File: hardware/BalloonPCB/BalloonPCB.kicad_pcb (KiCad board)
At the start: 2 copper layers, 106.7 x 86.4 mm, 5 parts, among them P1 BMP180_HEADER, P2 GPS_HEADER, P3 ACCEL_HEADER, P4 CONN_01X24, U1 Teensy3.5

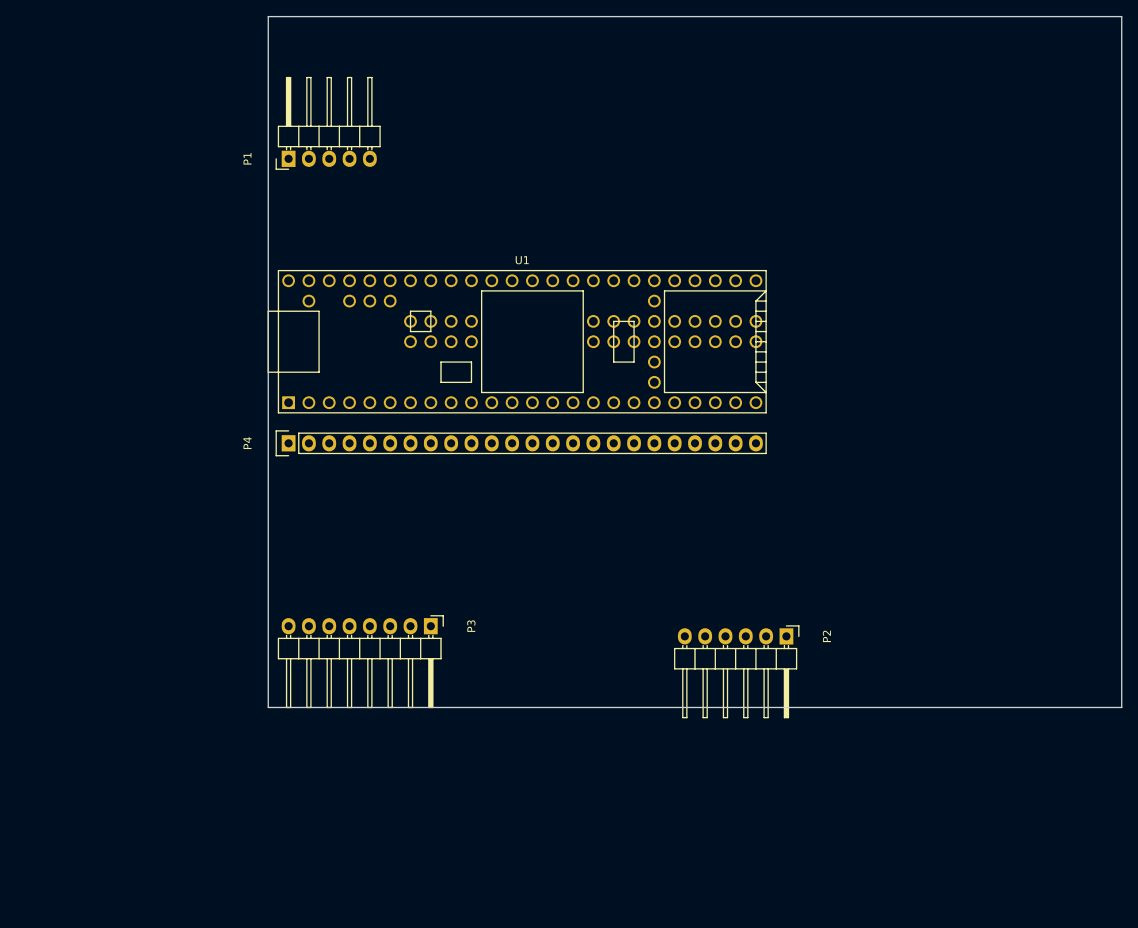
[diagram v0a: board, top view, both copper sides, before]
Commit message: First routing pass, everything except radio
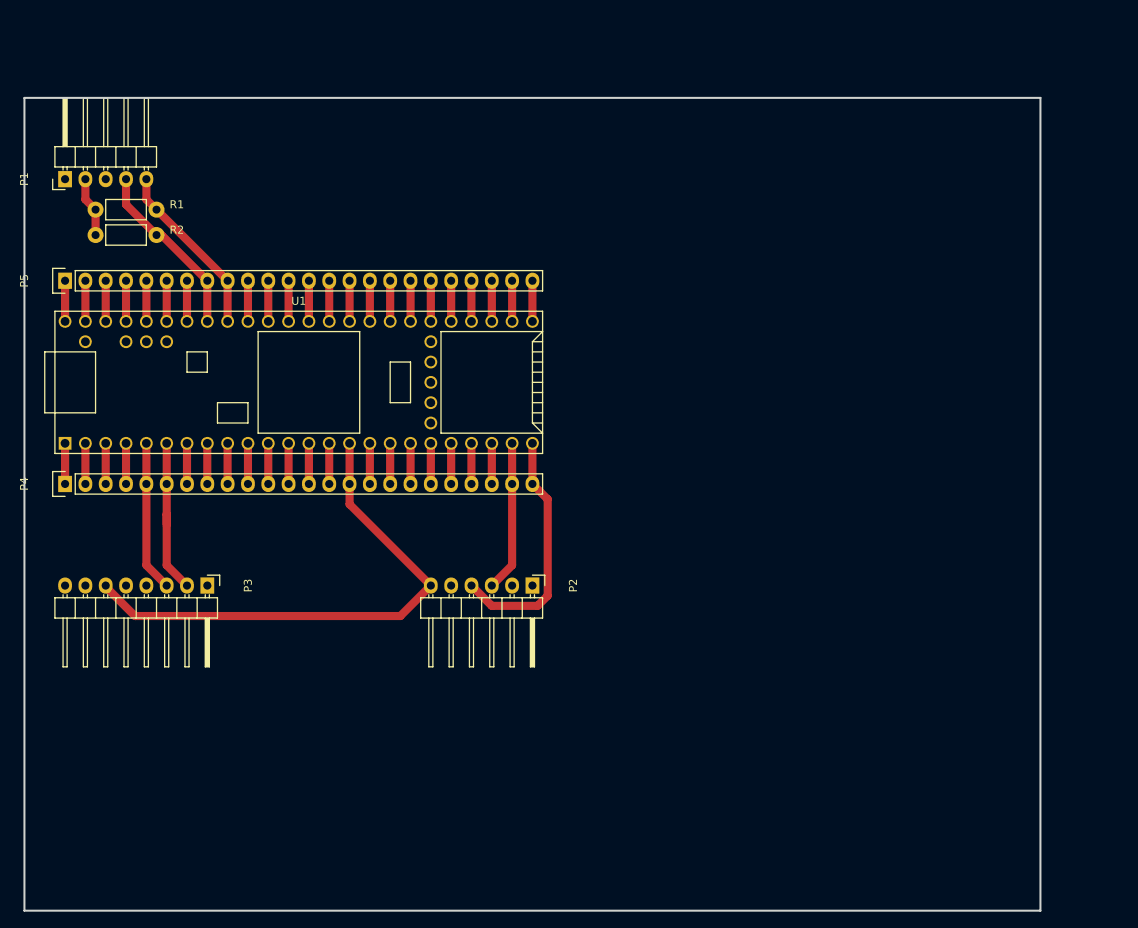
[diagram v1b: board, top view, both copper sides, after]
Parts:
- added P5: CONN_01X24, Pin_Headers:Pin_Header_Straight_1x24, F.Cu at (55.9, 73.7)
- added R1: 3.3k, Resistors_THT:Resistor_Horizontal_RM7mm, F.Cu at (59.7, 64.8)
- added R2: 3.3k, Resistors_THT:Resistor_Horizontal_RM7mm, F.Cu at (59.7, 67.9)
- moved P2 32.4 mm to (114.3, 111.8)
- moved P3 28.4 mm to (73.7, 111.8)
- moved U1 28.4 mm to (85.1, 86.4)
- moved P4 28.4 mm to (55.9, 99.1)
- moved P1 28.1 mm to (55.9, 61.0)
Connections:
- P3 pad 2: SDA0 -> SDA2
- P3 pad 3: SCL0 -> SCL2
- P4 pad 1: Net-(P4-Pad1) -> GND
- P4 pad 5: Net-(P4-Pad5) -> SCL2
- P4 pad 6: Net-(P4-Pad6) -> SDA2
- U1 pad 1: Net-(P4-Pad1) -> GND
- U1 pad 26: Net-(U1-Pad26) -> +3V3
- U1 pad 45: Net-(U1-Pad45) -> SDA0
- U1 pad 46: Net-(U1-Pad46) -> SCL0
- U1 pad 5: Net-(P4-Pad5) -> SCL2
- U1 pad 6: Net-(P4-Pad6) -> SDA2
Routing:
- net +3V3: track 0.00 -> 73.4 mm
- net GPS_RXD: track 0.00 -> 30.9 mm
- net SCL0: track 0.00 -> 22.4 mm
- net SDA0: track 0.00 -> 22.0 mm
- net SDA2: track 0.00 -> 20.1 mm
- net GPS_TXD: track 0.00 -> 18.8 mm
- net SCL2: track 0.00 -> 18.8 mm
- net GND: track 0.00 -> 10.2 mm
- net Net-(P5-Pad7): track 0.00 -> 5.08 mm
- net Net-(P5-Pad6): track 0.00 -> 5.08 mm
- net Net-(P5-Pad5): track 0.00 -> 5.08 mm
- net Net-(P5-Pad4): track 0.00 -> 5.08 mm
- net Net-(P5-Pad3): track 0.00 -> 5.08 mm
- net Net-(P5-Pad24): track 0.00 -> 5.08 mm
- net Net-(P5-Pad23): track 0.00 -> 5.08 mm
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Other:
- board size 106.7 x 86.4 mm -> 127 x 101.6 mm
- net class Default: trace_width 0.254 -> 1.016
- net class Power added: clearance 0.254, trace_width 1.016, via_dia 0.762, via_drill 0.3302
- net class Signal added: clearance 0.254, trace_width 0.508, via_dia 0.762, via_drill 0.3302
- net class SmallSig added: clearance 0.254, trace_width 0.254, via_dia 0.762, via_drill 0.3302

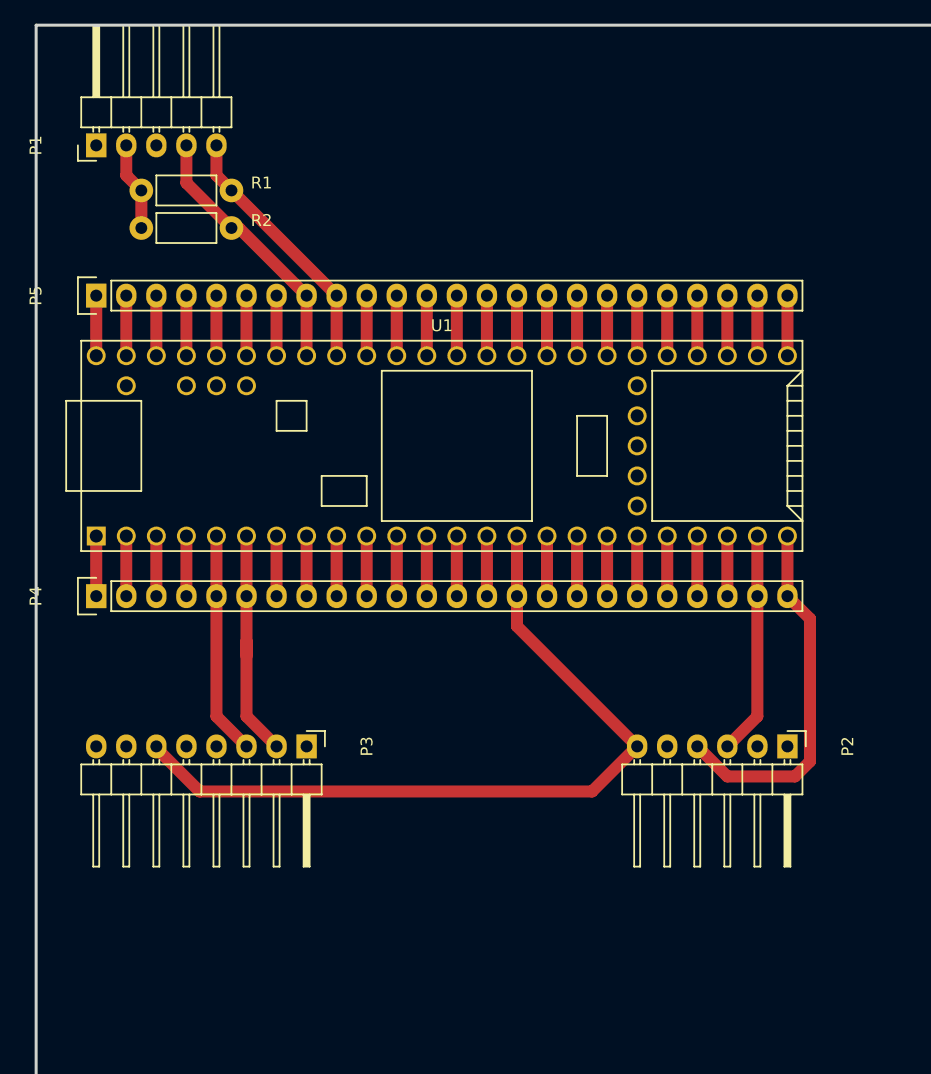
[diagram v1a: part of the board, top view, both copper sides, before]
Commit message: PCB signals routed
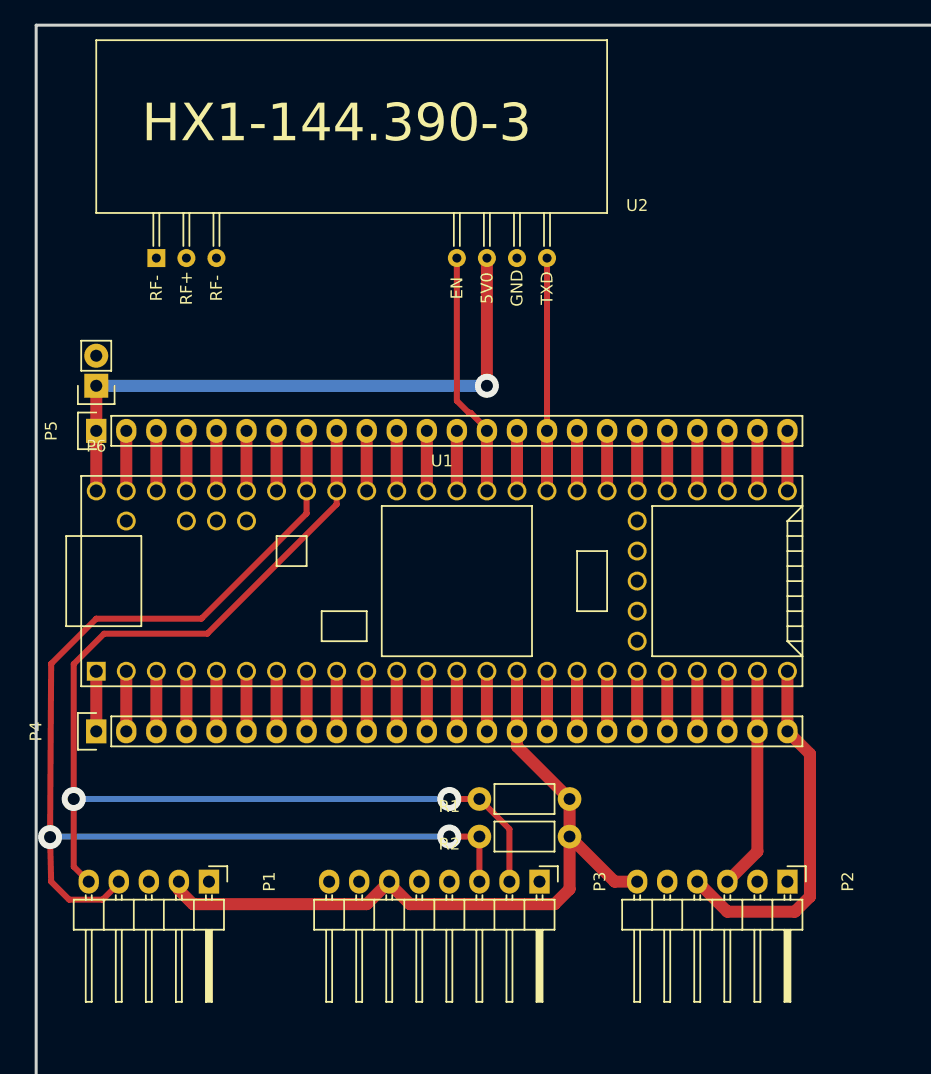
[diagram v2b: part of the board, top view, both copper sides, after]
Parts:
- added P6: 5VDC_HEADER, Pin_Headers:Pin_Header_Straight_1x02, F.Cu at (55.9, 81.3)
- added U2: HX1, HX1:HX1, F.Cu at (55.9, 66.7)
- moved P1 63.0 mm to (65.4, 123.2), turned to 270 degrees
- moved R1 62.9 mm to (95.9, 116.2), turned to 180 degrees
- moved R2 62.9 mm to (95.9, 119.4), turned to 180 degrees
- moved P3 22.8 mm to (93.3, 123.2)
- moved P5 11.4 mm to (55.9, 85.1)
- moved U1 11.4 mm to (85.1, 97.8)
- moved P2 11.4 mm to (114.3, 123.2)
- moved P4 11.4 mm to (55.9, 110.5)
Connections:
- net Net-(P5-Pad1) renamed +5V
- net Net-(P5-Pad14) renamed TX_EN
- net Net-(P5-Pad16) renamed TXD
- P3 pad 2: SDA2 -> SDA0
- P3 pad 3: SCL2 -> SCL0
- P5 pad 3: Net-(P5-Pad3) -> +3V3
- U1 pad 51: Net-(P5-Pad3) -> +3V3
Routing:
- net SCL0: track 22.4 -> 99.6 mm, vias 0 -> 2
- net SDA0: track 22.0 -> 95.4 mm, vias 0 -> 2
- net +5V: track 5.08 -> 52.7 mm, vias 0 -> 1
- net TX_EN: track 5.08 -> 20.8 mm
- net SDA2: track 20.1 -> 5.08 mm
- net TXD: track 5.08 -> 19.7 mm
- net SCL2: track 18.8 -> 5.08 mm
- net Net-(P5-Pad3): track 5.08 -> 0.00 mm
- net +3V3: track 73.4 -> 69.0 mm
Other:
- net class Default: via_dia 0.762 -> 2.032; via_drill 0.3302 -> 1.016
- net class Power: via_dia 0.762 -> 2.032; via_drill 0.3302 -> 1.016
- net class Signal: via_dia 0.762 -> 2.032; via_drill 0.3302 -> 1.016
- net class SmallSig: via_dia 0.762 -> 2.032; via_drill 0.3302 -> 1.016

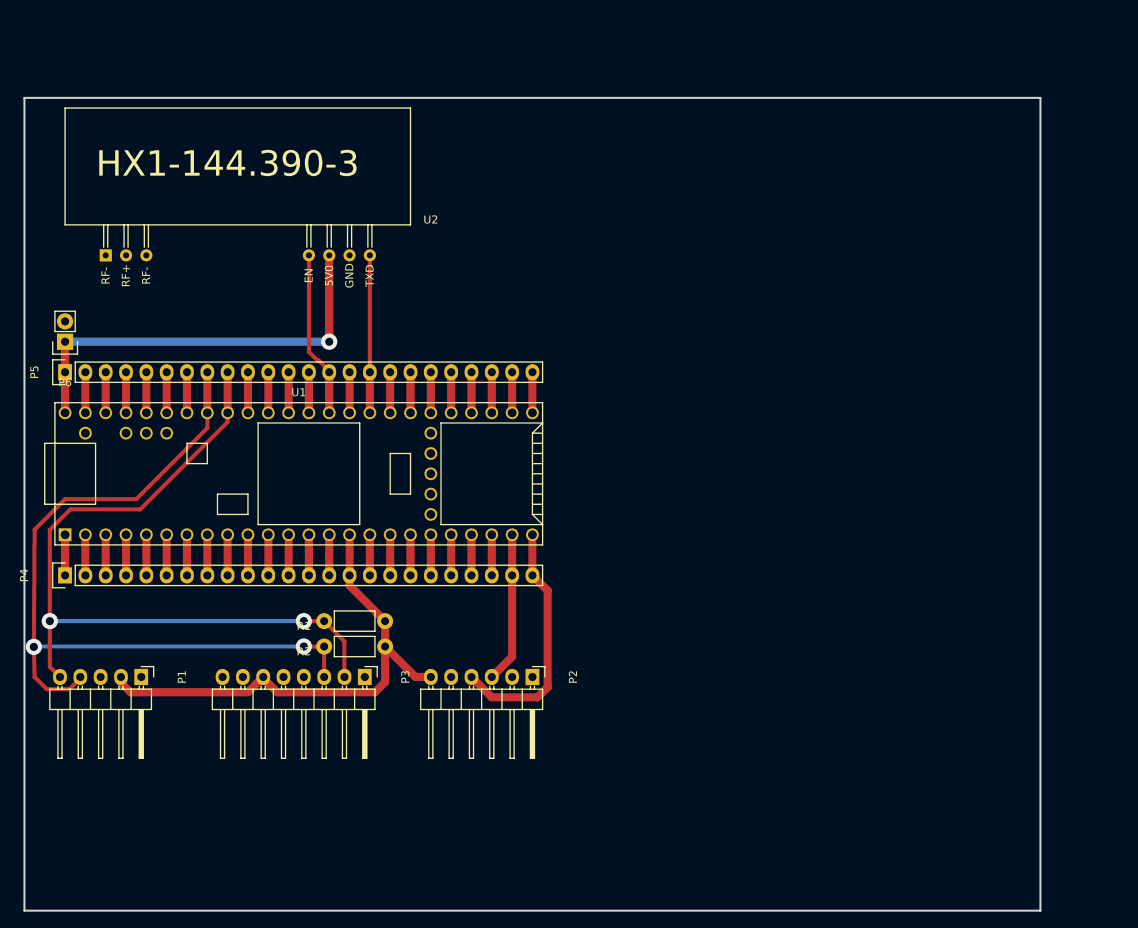
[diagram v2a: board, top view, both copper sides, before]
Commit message: Board fully routed, add decoupling caps
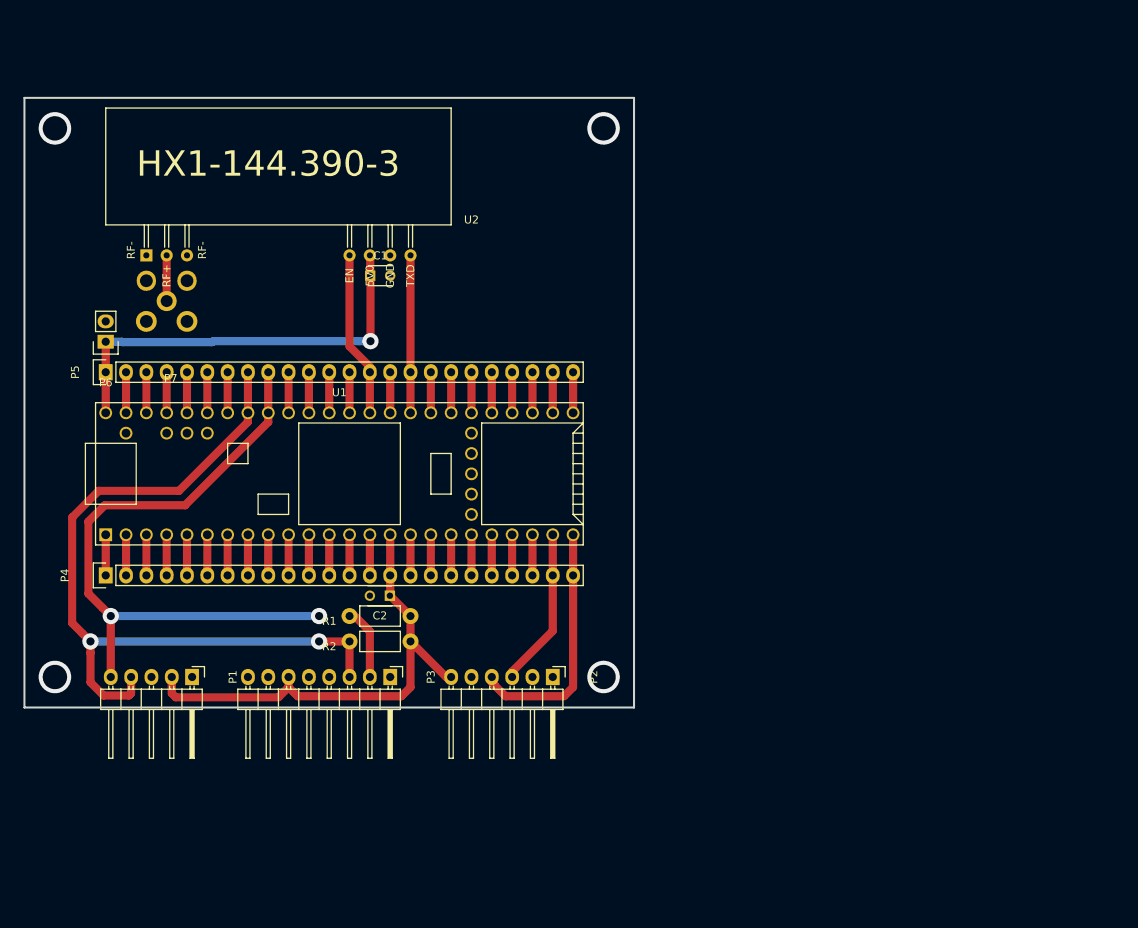
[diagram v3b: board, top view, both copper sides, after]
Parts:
- added C1: 0.1uF, Capacitors_THT:C_Disc_D3_P2.5, F.Cu at (94.0, 73.0)
- added C2: 0.1uF, Capacitors_THT:C_Disc_D3_P2.5, F.Cu at (96.5, 113.0)
- added P7: SMA, Connectors_TE-Connectivity:SMA_Socket_TYCO-AMP, F.Cu at (68.6, 76.2)
- moved P1 6.35 mm to (71.8, 123.2)
- moved P4 5.08 mm to (61.0, 110.5)
- moved P5 5.08 mm to (61.0, 85.1)
- moved P6 5.08 mm to (61.0, 81.3)
- moved U1 5.08 mm to (90.2, 97.8)
- moved U2 5.08 mm to (61.0, 66.7)
- moved R1 3.24 mm to (99.1, 115.6)
- moved R2 3.24 mm to (99.1, 118.7)
- moved P3 3.17 mm to (96.5, 123.2)
- moved P2 2.54 mm to (116.8, 123.2)
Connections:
- U2 pad 1: Net-(U2-Pad1) -> RF-
- U2 pad 2: Net-(U2-Pad2) -> RF+
- U2 pad 3: Net-(U2-Pad3) -> RF-
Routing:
- net RF+: track 0.00 -> 5.72 mm
- net SDA0: track 95.4 -> 89.7 mm
- net +3V3: track 69.0 -> 67.0 mm
- net GPS_TXD: track 18.8 -> 20.5 mm
- net (no net): vias 0 -> 4
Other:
- board size 127 x 101.6 mm -> 76.2 x 76.2 mm
- net class Default: clearance 0.254 -> 0.79375
- net class Mounting Holes added: clearance 0.79375, trace_width 1.016, via_dia 4.064, via_drill 3.048
- net class Power: clearance 0.254 -> 0.79375
- net class Signal: clearance 0.254 -> 0.79375; trace_width 0.508 -> 1.016
- net class SmallSig removed
- rule trace_clearance: 0.254 -> 0.79375
- rule trace_min: 0.254 -> 0.8128
- rule via_min_drill: 0.3302 -> 0.4064
- rule via_min_size: 0.762 -> 0.8128

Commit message: Add pours
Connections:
- P7 pad 2: RF- -> GND
- U2 pad 1: RF- -> GND
- U2 pad 3: RF- -> GND
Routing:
- net GPS_RXD: track 31.1 -> 51.8 mm, vias 0 -> 2
- net GND: track 10.2 -> 16.5 mm
- net SDA0: track 89.7 -> 93.5 mm
- net SCL0: track 99.6 -> 98.8 mm
- net GPS_TXD: track 20.5 -> 21.2 mm, vias 0 -> 2
- net (no net): vias 4 -> 0
- added copper zone on B.Cu, net GND

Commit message: Add spot for thermristor
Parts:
- added P8: THERMO_HEADER, Connectors_Molex:Molex_KK-6410-02_02x2.54mm_Straight, F.Cu at (111.8, 81.3)
- added R3: 10k, Resistors_THT:Resistor_Horizontal_RM7mm, F.Cu at (111.8, 100.3)
- P6: footprint Pin_Headers:Pin_Header_Straight_1x02 -> Connectors_Molex:Molex_KK-6410-02_02x2.54mm_Straight
- moved P6 6.87 mm to (55.2, 85.1), turned to 90 degrees
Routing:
- net +3V3: track 66.6 -> 84.6 mm
- net Net-(P5-Pad21): track 5.08 -> 11.4 mm
- net +5V: track 52.9 -> 58.6 mm, vias 1 -> 2
